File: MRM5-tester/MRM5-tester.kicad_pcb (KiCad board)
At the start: 2 copper layers, 76 parts, among them IC1 STM32G051F8P6, IC2 OPA567AIRHGT, IC3 LM1085IS-3.3/NOPB, IC4 OPA567AIRHGT, J1 Conn_01x05, J2 GSB1C41110SSHR, J3 Conn_01x02, J4 Conn_01x02, Q1 MMBT3906-TP, Q2 MMBT3906-TP, Q3 MMBT3906-TP, Q4 MMBT3906-TP, T1 ZMPT107-1, U1 CP2102N-A02-GQFN20, U2 ADA4528-2ACPZ

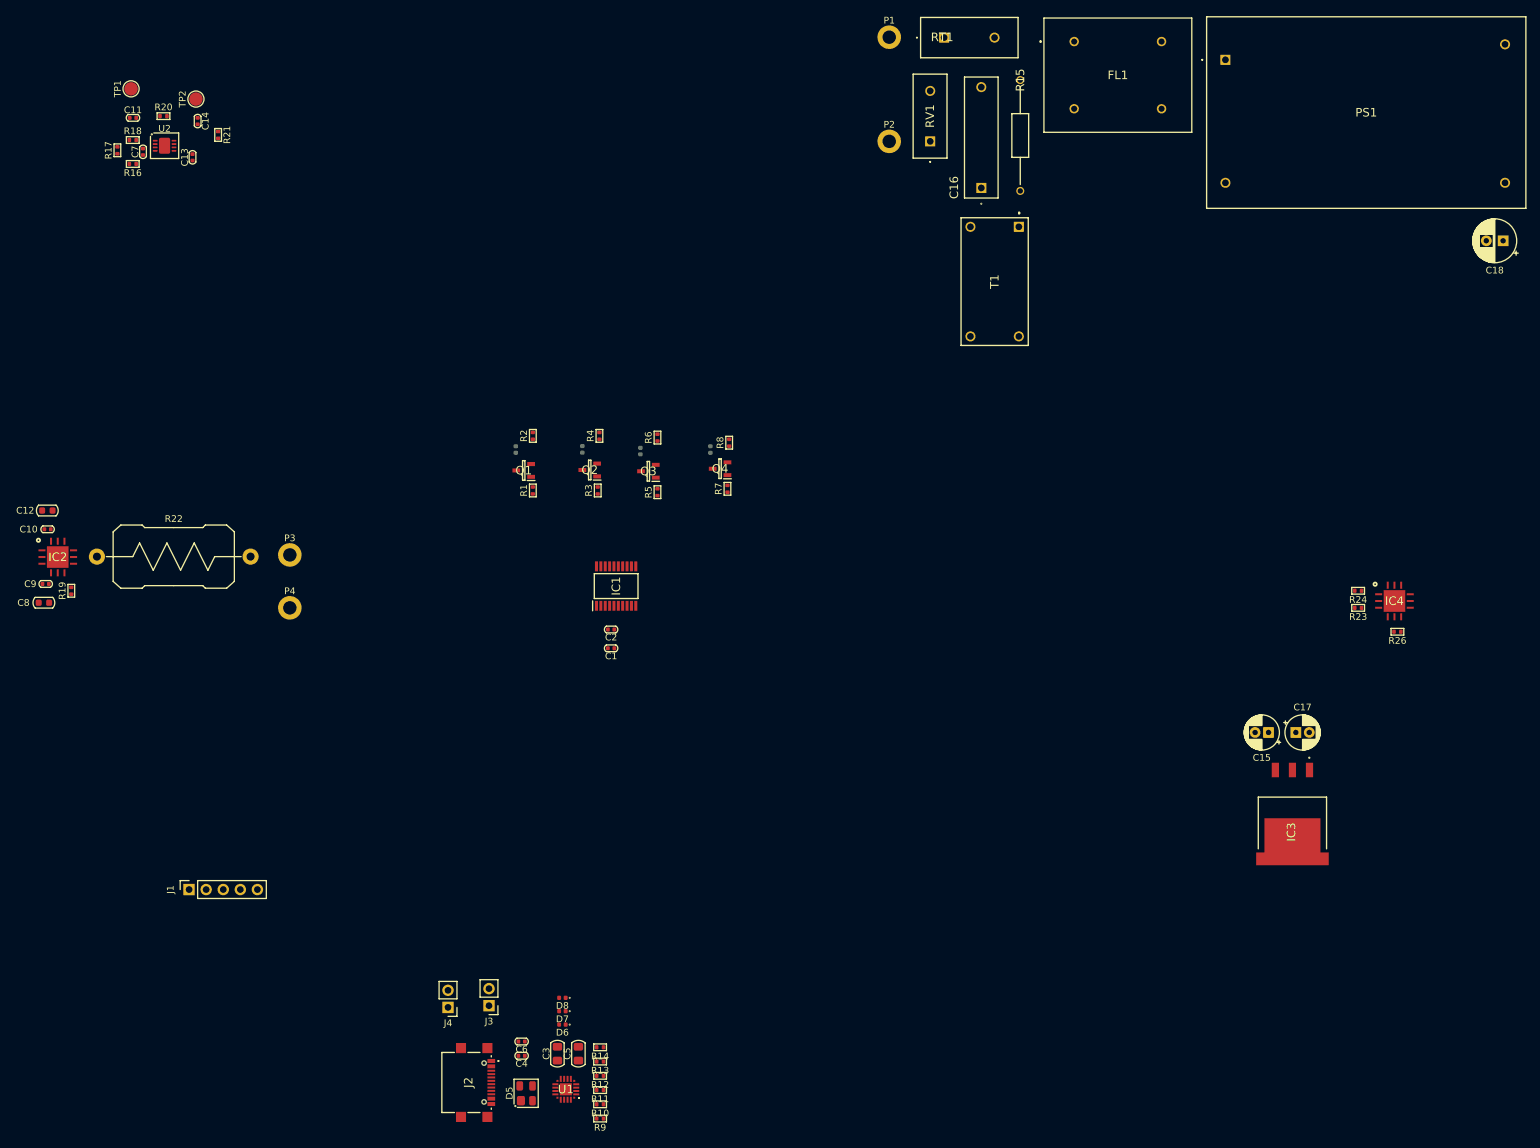
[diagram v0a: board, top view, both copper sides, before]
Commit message: tester pcb 디자인 완료
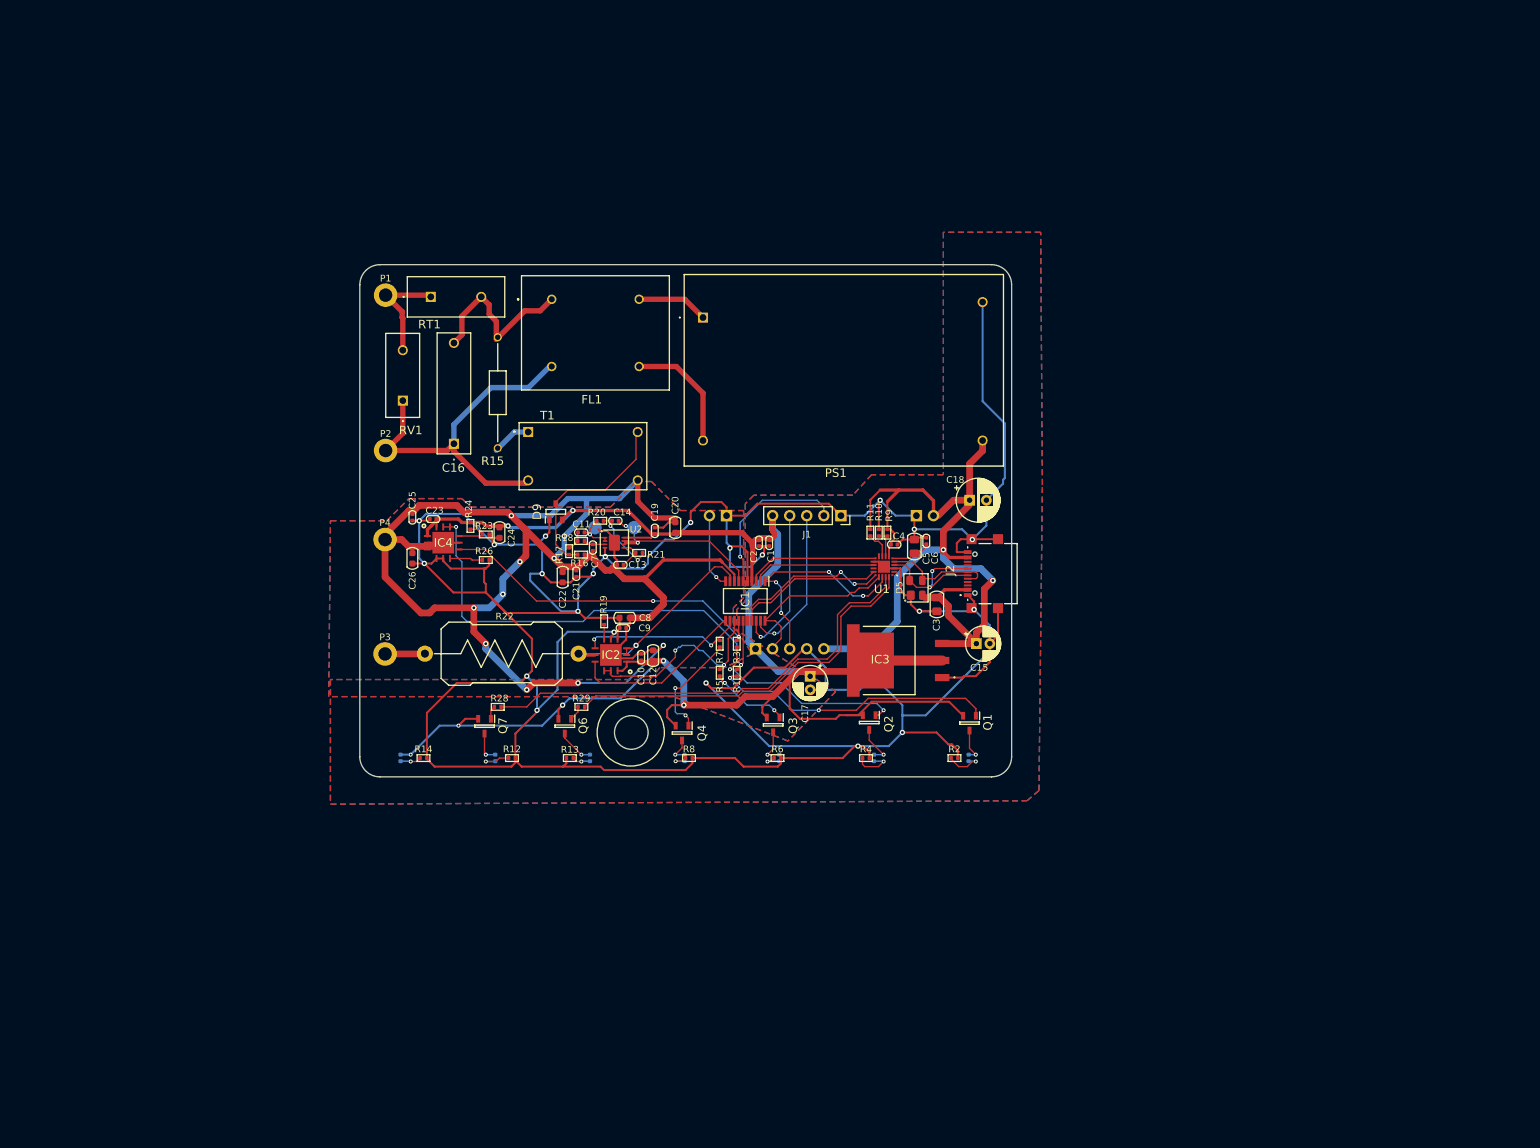
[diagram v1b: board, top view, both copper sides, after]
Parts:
- added C19: 100n, PCM_Capacitor_SMD_AKL:C_0402_1005Metric, F.Cu at (146.2, 102.1)
- added C20: 47u, PCM_Capacitor_SMD_AKL:C_0603_1608Metric, F.Cu at (149.3, 101.6)
- added C21: 100n, PCM_Capacitor_SMD_AKL:C_0402_1005Metric, F.Cu at (134.6, 108.5)
- added C22: 47u, PCM_Capacitor_SMD_AKL:C_0603_1608Metric, F.Cu at (132.5, 109.0)
- added C23: 100n, PCM_Capacitor_SMD_AKL:C_0402_1005Metric, F.Cu at (113.3, 100.3)
- added C24: 47u, PCM_Capacitor_SMD_AKL:C_0603_1608Metric, F.Cu at (123.1, 102.3)
- added C25: 100n, PCM_Capacitor_SMD_AKL:C_0402_1005Metric, F.Cu at (110.2, 100.1)
- added C26: 47u, PCM_Capacitor_SMD_AKL:C_0603_1608Metric, F.Cu at (110.2, 106.2)
- added D9: BAT54S, Mouser:SOT95P240X120-3N, F.Cu at (131.5, 99.2)
- added J5: Conn_01x05, Connector_PinSocket_2.54mm:PinSocket_1x05_P2.54mm_Vertical, B.Cu at (161.2, 119.6)
- added Q6: MMBT3906-TP, Mouser:SOT95P237X125-3N, F.Cu at (132.9, 131.1)
- added Q7: MMBT3906-TP, Mouser:SOT95P237X125-3N, F.Cu at (120.9, 131.1)
- added R28: 1k, PCM_Resistor_SMD_AKL:R_0402_1005Metric, F.Cu at (122.9, 128.3)
- added R29: 1k, PCM_Resistor_SMD_AKL:R_0402_1005Metric, F.Cu at (135.3, 128.3)
- D1, D2, D3, D4: value LED-WHITE -> LED-RED
- D6, D7, D8, J3, J4, TP1, TP2: moved to B.Cu
- moved IC4 141.8 mm to (114.8, 103.8)
- moved R26 136.0 mm to (121.1, 106.4), turned to 0 degrees
- moved R24 132.4 mm to (118.8, 101.3), turned to -90 degrees
- moved R23 130.2 mm to (121.1, 102.6), turned to 0 degrees
- moved J1 111.8 mm to (173.9, 99.8), turned to -90 degrees
- moved J2 108.5 mm to (196.2, 108.4), turned to 90 degrees
- moved R9 97.1 mm to (180.8, 102.3), turned to 90 degrees
- moved J3 96.7 mm to (185.2, 99.8), turned to -90 degrees
- moved C6 95.8 mm to (186.6, 103.6), turned to -90 degrees
- moved TP1 95.0 mm to (137.4, 101.6)
- moved D5 95.0 mm to (185.1, 110.6)
- moved R10 94.6 mm to (179.6, 102.3), turned to -90 degrees
- moved C4 94.1 mm to (181.9, 104.1)
- moved C12 92.7 mm to (146.0, 120.6), turned to 90 degrees
- moved R11 92.2 mm to (178.3, 102.3), turned to 90 degrees
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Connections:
- net Net-(PS1-AC_1) renamed /power/FL1_out1_sh
- net Net-(PS1-AC_2) renamed /power/FL1_out2_sh
- net Net-(R15-Pad2) renamed /analog/Vp_ssh
- C17 pad 1: /interface/3V3 -> /analog/3V3
- D8 pad 2: /interface/3V3 -> /analog/3V3
- IC1 pad 9: unconnected-(IC1-PA2-Pad9) -> /analog/Zfreed
- IC2 pad 2: Net-(IC2--IN) -> /analog/Zfreed
- IC2 pad 3: Net-(IC2--IN) -> /analog/Zfreed
- IC2 pad 8: Net-(IC2--IN) -> /analog/Zfreed
- IC3 pad 2: /interface/3V3 -> /analog/3V3
- IC3 pad 4: /interface/3V3 -> /analog/3V3
- IC4 pad 1: /interface/3V3 -> /analog/3V3
- IC4 pad 12: /interface/3V3 -> /analog/3V3
- J1 pad 5: /interface/3V3 -> /analog/3V3
- R22 pad 1: Net-(IC2--IN) -> /analog/Zfreed
- R24 pad 1: /interface/3V3 -> /analog/3V3
- U1 pad 19: Net-(D6-A) -> Net-(U1-~{RXT}/GPIO.3)
- U1 pad 20: Net-(D7-A) -> Net-(U1-~{TXT}/GPIO.2)
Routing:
- net GND: track 0.00 -> 581.0 mm, vias 0 -> 22
- net /analog/3V3: track 0.00 -> 262.9 mm, vias 0 -> 7
- net /analog/1V6: track 0.00 -> 241.0 mm, vias 0 -> 10
- net /interface/5V: track 0.00 -> 128.3 mm, vias 0 -> 2
- net /mcu/1V6_TFlag: track 0.00 -> 70.6 mm, vias 0 -> 2
- net Net-(U1-~{RXT}/GPIO.3): track 0.00 -> 69.0 mm
- net Net-(U1-~{TXT}/GPIO.2): track 0.00 -> 57.2 mm
- net /analog/Vn_h: track 0.00 -> 54.4 mm
- net /mcu/1V6_IFlag: track 0.00 -> 50.0 mm, vias 0 -> 2
- net Net-(Q1-B): track 0.00 -> 42.1 mm, vias 0 -> 2
- net /analog/Zfreed: track 0.00 -> 34.4 mm, vias 0 -> 1
- net /interface/UART_TXD: track 0.00 -> 33.5 mm, vias 0 -> 4
- net Net-(Q2-B): track 0.00 -> 30.6 mm, vias 0 -> 2
- net /analog/Z_TFlag: track 0.00 -> 30.4 mm, vias 0 -> 2
- net Net-(D9-A/K): track 0.00 -> 29.0 mm
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- added copper zone on B.Cu, net /analog/1V6
- added copper zone on F.Cu, net /analog/1V6
- added copper zone on B.Cu, net GND
- added copper zone on F.Cu, net GND
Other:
- board outline added: 97 x 76.2 mm
- board text added: "1V6IFlag"
- board text added: "1V6TFlag"
- board text added: "PWR"
- board text added: "RXT"
- board text added: "TXT"
- board text added: "Z_IFlag"
- board text added: "Z_TFlag"

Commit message: tester PCB 검토
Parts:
- added Debbit: ktw07182@gmail.com, Mouser:ktw07182_logo, B.Cu at (175.0, 71.8)
- added J6: Conn_01x02, Connector_PinHeader_2.54mm:PinHeader_1x02_P2.54mm_Vertical, B.Cu at (174.0, 104.0)
- added TP3: Z, TestPoint:TestPoint_Pad_D2.0mm, B.Cu at (139.5, 120.5)
- C15, C17: footprint Capacitor_THT:CP_Radial_D5.0mm_P2.00mm -> Capacitor_THT:C_Radial_D5.0mm_H11.0mm_P2.00mm
- C18: value 220uF_10V -> 220uF 16V 105℃; footprint Capacitor_THT:CP_Radial_D6.3mm_P2.50mm -> Capacitor_THT:C_Radial_D6.3mm_H11.0mm_P2.50mm
- J1: moved to B.Cu
- TP2: value V1 -> V
- moved PS1 0.44 mm to (153.2, 70.8)
- moved FL1 0.20 mm to (130.8, 67.8)
- turned J1 to 90 degrees
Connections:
- IC1 pad 2: /interface/WAKEUP -> /interface/PUSH_BTN
- U1 pad 13: /interface/WAKEUP -> unconnected-(U1-~{WAKEUP}-Pad13)
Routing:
- net GND: track 581.0 -> 646.0 mm, vias 22 -> 28
- net /analog/1V6: track 241.0 -> 292.8 mm
- net /interface/PUSH_BTN: track 0.00 -> 19.3 mm, vias 0 -> 1
- net /interface/WAKEUP: track 18.4 -> 0.00 mm
- net /interface/STLINK_RST: track 24.4 -> 28.6 mm
- net /analog/Vn_h: track 54.4 -> 53.4 mm
- net /mcu/1V6_IFlag: track 50.0 -> 50.7 mm
- net /analog/3V3: track 262.9 -> 262.2 mm
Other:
- outline, holes or cut-outs redrawn
- board text added: "+"
- board text added: "Calibration"
- board text added: "Signal Test"
- board text added: "Standard Current Generator (mA)"
- board text added: "V1"
- board text added: "V1.0.0"
- board text added: "V2"
- board text added: "Z"

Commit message: MRM5-tester updated
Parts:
- removed the C15 at (194.1, 118.9)
- removed the C17 at (169.4, 123.7)
- removed the D1 at (192.9, 135.9)
- removed the D2 at (178.9, 135.9)
- removed D3, D4: LED-RED, LED_SMD:LED_0402_1005Metric
- removed D6: LED-YELLOW, LED_SMD:LED_0402_1005Metric
- removed D7: LED-GREEN, LED_SMD:LED_0402_1005Metric
- removed D8: LED-WHITE, LED_SMD:LED_0402_1005Metric
- removed the IC3 at (176.3, 121.4)
- removed the J2 at (196.2, 108.4)
- added C19: 10uF, 16V, PCM_Capacitor_SMD_AKL:C_0603_1608Metric, F.Cu at (194.1, 120.2)
- added C24: 10uF, 16V, PCM_Capacitor_SMD_AKL:C_0603_1608Metric, F.Cu at (170.2, 125.0)
- added IC5: LD1085D2T33R, Mouser:LD1085D2T33R, F.Cu at (179.7, 122.7)
- added J4: GSB1C41110SSHR, Mouser:GSB1C41110SSHR, F.Cu at (196.1, 108.5)
- added LED1: LED_0603_Red, PCM_LED_SMD_AKL:LED_0603_1608Metric, B.Cu at (192.8, 135.9)
- added LED2: LED_0603_Red, PCM_LED_SMD_AKL:LED_0603_1608Metric, B.Cu at (178.7, 135.9)
- added LED3: LED_0603_Red, PCM_LED_SMD_AKL:LED_0603_1608Metric, B.Cu at (164.7, 135.9)
- added LED4: LED_0603_Red, PCM_LED_SMD_AKL:LED_0603_1608Metric, B.Cu at (150.6, 135.9)
- added LED5: LED_0603_Red, PCM_LED_SMD_AKL:LED_0603_1608Metric, B.Cu at (122.5, 135.9)
- added LED6: LED_0603_Green, PCM_LED_SMD_AKL:LED_0603_1608Metric, B.Cu at (136.6, 135.9)
- added LED7: LED_0603_White, PCM_LED_SMD_AKL:LED_0603_1608Metric, B.Cu at (108.5, 135.9)
- D1: renamed from D5; value SP0503BAHT -> CD143A-SR05; footprint PCM_Package_TO_SOT_SMD_AKL:SOT-143 -> Package_TO_SOT_SMD:SOT-143_Handsoldering
- FL1: value SSHB10HS-R11100 -> SS21V-R110100
- R17: renamed from R15; value MBB02070C1004FCT00 -> 1MΩ 1W
- U2: value ADA4528-2ACPZ -> ADA4661-2ACPZ-RL
- moved Q2 1.65 mm to (178.1, 132.2)
- renumbered C9 to C10, C22 to C11, C10 to C12, C11 to C13, C19 to C14, C12 to C15, C20 to C16, C13 to C17, C14 to C18, C16 to C20, C23 to C21, C24 to C22, C26 to C23, C18 to C26, C21 to C9, D9 to D2, IC4 to IC3, J6 to J2, J5 to J3, J3 to J5, J4 to J6, Q7 to Q5, R28 to R12, R12 to R13, R29 to R14, R13 to R15, R14 to R16, R16 to R18, R17 to R19, R18 to R20, R19 to R21, R20 to R22, R21 to R23, R22 to R24, R23 to R25, R24 to R26, R26 to R27, Debbit to Symbol1, TP3 to TP2, TP2 to TP3
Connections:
- D1 pad 2: /interface/5V -> Net-(D1-L1)
- D1 pad 4: Net-(D5-L3) -> /interface/5V
- U1 pad 4: Net-(D5-L3) -> Net-(D1-L1)
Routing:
- net Net-(D1-L1): track 0.00 -> 23.2 mm, vias 0 -> 2
- net Net-(D5-L3): track 22.0 -> 0.00 mm, vias 2 -> 0
- net GND: track 646.0 -> 659.4 mm, vias 28 -> 31
- net /analog/1V6: track 292.8 -> 297.3 mm
- net Net-(Q2-B): track 30.6 -> 34.2 mm
- net Net-(LED2-A): track 5.99 -> 4.45 mm
- net /analog/3V3: track 262.2 -> 263.2 mm
- net /interface/5V: track 127.8 -> 128.5 mm, vias 2 -> 3

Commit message: case updated
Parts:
- added L1: 744770218, Mouser:WE-PD_744770218, F.Cu at (110.3, 130.2)
- moved R16 7.31 mm to (119.1, 135.8)
- moved Q5 3.40 mm to (124.3, 130.8)
- moved R12 2.86 mm to (125.7, 128.2)
- moved R24 2.11 mm to (135.0, 118.2)
- moved P3 0.90 mm to (106.0, 119.5)
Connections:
- P3 pad 1: Net-(P3-Pad1) -> Net-(L1-Pad2)
- R24 pad 2: Net-(P3-Pad1) -> Net-(L1-Pad1)
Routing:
- net GND: track 659.4 -> 645.5 mm
- net Net-(L1-Pad1): track 0.00 -> 13.3 mm
- net Net-(L1-Pad2): track 0.00 -> 11.0 mm
- net Net-(LED7-K): track 3.24 -> 10.8 mm
- net Net-(P3-Pad1): track 5.94 -> 0.00 mm
- net Net-(U1-~{RXT}/GPIO.3): track 69.0 -> 66.2 mm
- net /analog/Zfreed: track 34.4 -> 36.3 mm
- net Net-(LED5-A): track 4.62 -> 6.16 mm
- net /analog/3V3: track 263.2 -> 261.8 mm

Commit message: tester pcb updated
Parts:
- added J4: PINHD_1x2_Female, Connector_PinSocket_2.54mm:PinSocket_1x02_P2.54mm_Vertical, F.Cu at (151.9, 99.8)
- J1: renamed from J2; moved to F.Cu
- J2: renamed from J6; moved to F.Cu
- J5: value Conn_01x02 -> PINHD_1x2_Female; footprint Connector_PinHeader_2.54mm:PinHeader_1x02_P2.54mm_Vertical -> Connector_PinSocket_2.54mm:PinSocket_1x02_P2.54mm_Vertical; moved to F.Cu
- J6: renamed from J1; moved to F.Cu
- J7: renamed from J3; moved to F.Cu
- LED1, LED2, LED3, LED4, LED5: value LED_0603_Red -> LED_5mm; footprint PCM_LED_SMD_AKL:LED_0603_1608Metric -> PCM_LED_THT_AKL:LED_D5.0mm; moved to F.Cu
- LED6: value LED_0603_Green -> LED_5mm; footprint PCM_LED_SMD_AKL:LED_0603_1608Metric -> PCM_LED_THT_AKL:LED_D5.0mm; moved to F.Cu
- LED7: value LED_0603_White -> LED_5mm; footprint PCM_LED_SMD_AKL:LED_0603_1608Metric -> PCM_LED_THT_AKL:LED_D5.0mm; moved to F.Cu
- Symbol1: moved to F.Cu
- moved Symbol1 38.3 mm to (169.7, 109.7), turned to 0 degrees
- moved J2 12.2 mm to (148.6, 108.7)
- moved LED7 11.2 mm to (119.6, 134.9), turned to 0 degrees
- moved R15 8.07 mm to (130.3, 128.5), turned to 90 degrees
- moved R2 6.93 mm to (183.9, 135.9), turned to -90 degrees
- moved LED4 6.90 mm to (157.5, 135.1), turned to 0 degrees
- moved Q2 6.89 mm to (171.9, 129.4)
- moved R13 6.61 mm to (128.5, 130.3)
- moved R16 6.57 mm to (119.4, 129.3), turned to 90 degrees
- moved LED1 6.43 mm to (186.4, 134.9), turned to 0 degrees
- moved LED5 6.35 mm to (128.8, 134.9), turned to 180 degrees
- moved LED6 3.87 mm to (132.8, 134.9), turned to 0 degrees
- moved Q3 3.63 mm to (167.1, 129.4)
- moved R8 3.61 mm to (154.9, 135.9), turned to -90 degrees
- moved R4 3.42 mm to (174.2, 135.9), turned to -90 degrees
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- renumbered IC5 to IC3, IC3 to IC4, J4 to J3
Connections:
- net Net-(D2-A/K) renamed /analog/V2p
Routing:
- net GND: track 645.5 -> 612.4 mm, vias 31 -> 27
- net /analog/1V6: track 297.3 -> 323.9 mm, vias 10 -> 12
- net /analog/3V3: track 261.8 -> 243.9 mm
- net /analog/V2p: track 29.0 -> 45.7 mm
- net Net-(Q2-B): track 34.2 -> 23.0 mm
- net Net-(LED4-A): track 3.92 -> 10.5 mm, vias 1 -> 0
- net Net-(LED7-K): track 10.8 -> 5.18 mm, vias 1 -> 0
- net Net-(LED2-A): track 4.45 -> 9.34 mm, vias 1 -> 0
- net /interface/SYNC: track 11.2 -> 6.82 mm
- net Net-(LED6-K): track 2.71 -> 6.89 mm, vias 1 -> 0
- net Net-(Q3-B): track 11.8 -> 15.0 mm
- net Net-(LED2-K): track 5.97 -> 2.84 mm, vias 1 -> 0
- net Net-(LED1-K): track 5.68 -> 2.75 mm, vias 1 -> 0
- net Net-(U1-~{TXT}/GPIO.2): track 57.2 -> 55.0 mm
- net Net-(U1-~{RXT}/GPIO.3): track 66.2 -> 64.8 mm
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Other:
- board text added: "3.3V 1A"
- board text added: "AC 220V"
- board text added: "CheckBox"
- board text added: "V1.0.0 2024.12.10."
- board text removed: "1V6IFlag"
- board text removed: "1V6TFlag"
- board text removed: "Calibration"
- board text removed: "PWR"
- board text removed: "RXT"
- board text removed: "Signal Test"
- board text removed: "Standard Current Generator (mA)"
- board text removed: "TXT"
- board text removed: "V1"
- board text removed: "V1.0.0"
- board text removed: "V2"
- board text removed: "Z"
- board text removed: "Z_IFlag"
- board text removed: "Z_TFlag"
